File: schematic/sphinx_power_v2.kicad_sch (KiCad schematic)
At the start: 0 parts

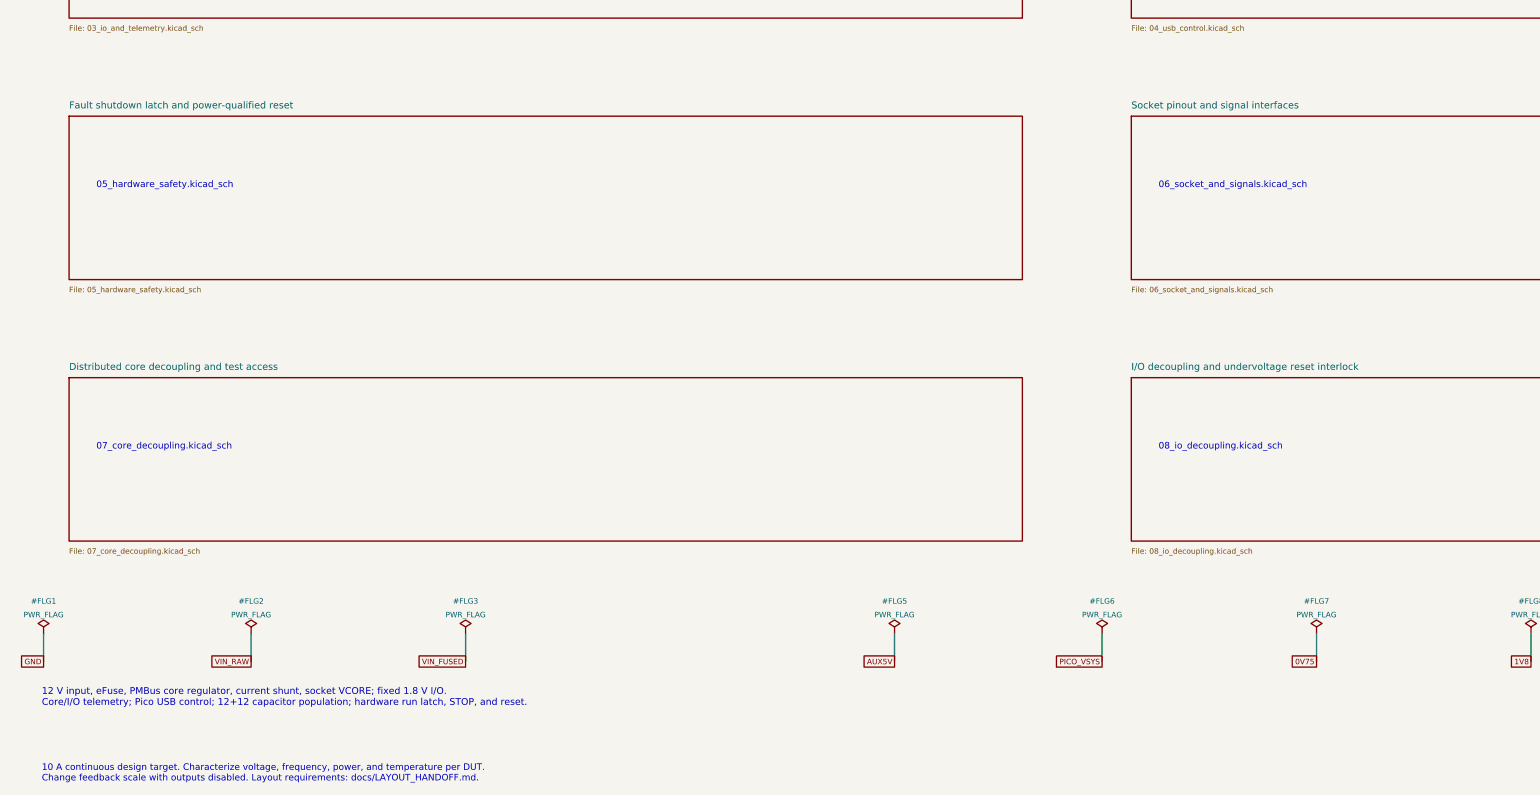
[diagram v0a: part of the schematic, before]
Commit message: Decouple DUT reset and input diagnostics from power interlocks
Use explicit manual, ZedBoard, and Pico reset requests. Route input-voltage validity to telemetry while retaining protective power interlocks. Synchronize requirements, schematic exports, BOM, and verification evidence.
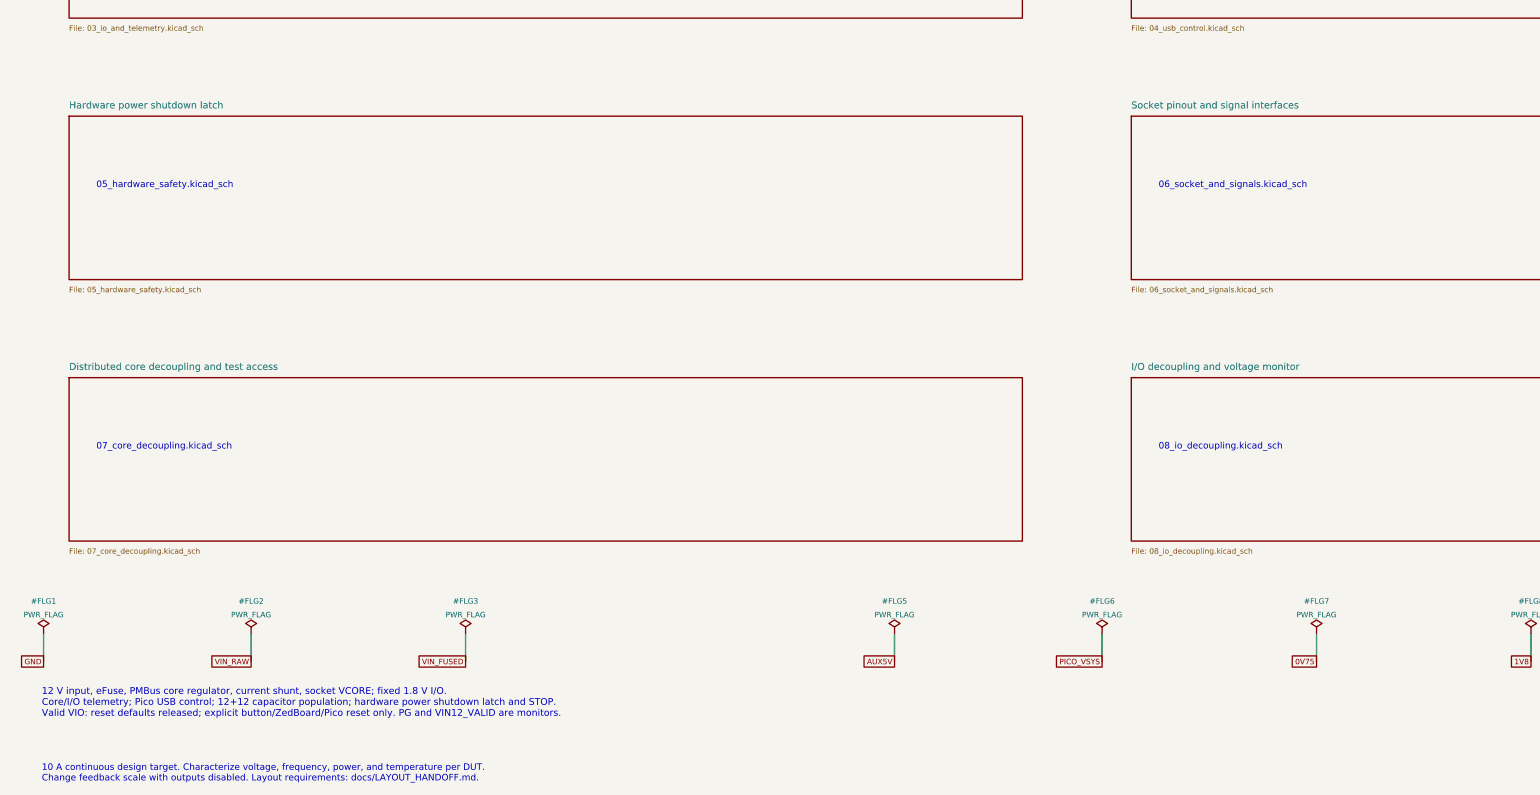
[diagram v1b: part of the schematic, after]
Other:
- sheet Fault shutdown latch and power-qualified reset renamed Hardware power shutdown latch
- sheet I/O decoupling and undervoltage reset interlock renamed I/O decoupling and voltage monitor
- note added: "12 V input, eFuse, PMBus core regulator, current shunt, socket VCORE; fixed 1.8 V I/O. Core/I/O telemetry; Pico USB control; 12+12 capacitor population; hardware power shutdown latch and STOP. Valid VIO: reset defaults released; explicit button/ZedBoard/Pico reset only. PG and VIN12_VALID are monitors."
- note removed: "12 V input, eFuse, PMBus core regulator, current shunt, socket VCORE; fixed 1.8 V I/O. Core/I/O telemetry; Pico USB control; 12+12 capacitor population; hardware run latch, STOP, and reset."
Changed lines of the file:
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@@
 (kicad_sch (version 20250114) (generator "eeschema") (generator_version "10.0")
  (paper "A3")
-        (title_block (title "Sphinx V2 | Programmable power test platform") (date "2026-09-19") (rev "V2")
+        (title_block (title "Sphinx V2 | Programmable power test platform") (date "2026-09-20") (rev "V2")
         (company "Sphinx | Programmable power test board")
         (comment 1 "Review package: PCB, PI, SI, thermal and ASIC limits require qualification")
@@
 (sheet (at 220 97) (size 175 30) (stroke (width 0.254) (type default)) (fill (color 0 0 0 0)) (property "Sheetname" "USB control and remote reset" (at 220 95.73 0) (effects (font (size 1.27 1.27)) (justify left bottom) )) (property "Sheetfile" "04_usb_control.kicad_sch" (at 220 128.27 0) (effects (font (size 1.0 1.0)) (justify left top) )) (instances (project "sphinx_power_v2" (path "/f39c8d6a-e478-5a84-9c95-766dfa82ae02" (page "5")))))
 (text "04_usb_control.kicad_sch" (at 225 109 0) (effects (font (size 1.2 1.2)) (justify left top) ))
-(sheet (at 25 145) (size 175 30) (stroke (width 0.254) (type default)) (fill (color 0 0 0 0)) (property "Sheetname" "Fault shutdown latch and power-qualified reset" (at 25 143.73 0) (effects (font (size 1.27 1.27)) (justify left bottom) )) (property "Sheetfile" "05_hardware_safety.kicad_sch" (at 25 176.27 0) (effects (font (size 1.0 1.0)) (justify left top) )) (instances (project "sphinx_power_v2" (path "/f39c8d6a-e478-5a84-9c95-766dfa82ae02" (page "6")))))
+(sheet (at 25 145) (size 175 30) (stroke (width 0.254) (type default)) (fill (color 0 0 0 0)) (property "Sheetname" "Hardware power shutdown latch" (at 25 143.73 0) (effects (font (size 1.27 1.27)) (justify left bottom) )) (property "Sheetfile" "05_hardware_safety.kicad_sch" (at 25 176.27 0) (effects (font (size 1.0 1.0)) (justify left top) )) (instances (project "sphinx_power_v2" (path "/f39c8d6a-e478-5a84-9c95-766dfa82ae02" (page "6")))))
 (text "05_hardware_safety.kicad_sch" (at 30 157 0) (effects (font (size 1.2 1.2)) (justify left top) ))
 (sheet (at 220 145) (size 175 30) (stroke (width 0.254) (type default)) (fill (color 0 0 0 0)) (property "Sheetname" "Socket pinout and signal interfaces" (at 220 143.73 0) (effects (font (size 1.27 1.27)) (justify left bottom) )) (property "Sheetfile" "06_socket_and_signals.kicad_sch" (at 220 176.27 0) (effects (font (size 1.0 1.0)) (justify left top) )) (instances (project "sphinx_power_v2" (path "/f39c8d6a-e478-5a84-9c95-766dfa82ae02" (page "7")))))
@@
 (sheet (at 25 193) (size 175 30) (stroke (width 0.254) (type default)) (fill (color 0 0 0 0)) (property "Sheetname" "Distributed core decoupling and test access" (at 25 191.73 0) (effects (font (size 1.27 1.27)) (justify left bottom) )) (property "Sheetfile" "07_core_decoupling.kicad_sch" (at 25 224.27 0) (effects (font (size 1.0 1.0)) (justify left top) )) (instances (project "sphinx_power_v2" (path "/f39c8d6a-e478-5a84-9c95-766dfa82ae02" (page "8")))))
 (text "07_core_decoupling.kicad_sch" (at 30 205 0) (effects (font (size 1.2 1.2)) (justify left top) ))
-(sheet (at 220 193) (size 175 30) (stroke (width 0.254) (type default)) (fill (color 0 0 0 0)) (property "Sheetname" "I/O decoupling and undervoltage reset interlock" (at 220 191.73 0) (effects (font (size 1.27 1.27)) (justify left bottom) )) (property "Sheetfile" "08_io_decoupling.kicad_sch" (at 220 224.27 0) (effects (font (size 1.0 1.0)) (justify left top) )) (instances (project "sphinx_power_v2" (path "/f39c8d6a-e478-5a84-9c95-766dfa82ae02" (page "9")))))
+(sheet (at 220 193) (size 175 30) (stroke (width 0.254) (type default)) (fill (color 0 0 0 0)) (property "Sheetname" "I/O decoupling and voltage monitor" (at 220 191.73 0) (effects (font (size 1.27 1.27)) (justify left bottom) )) (property "Sheetfile" "08_io_decoupling.kicad_sch" (at 220 224.27 0) (effects (font (size 1.0 1.0)) (justify left top) )) (instances (project "sphinx_power_v2" (path "/f39c8d6a-e478-5a84-9c95-766dfa82ae02" (page "9")))))
 (text "08_io_decoupling.kicad_sch" (at 225 205 0) (effects (font (size 1.2 1.2)) (justify left top) ))
-(text "12 V input, eFuse, PMBus core regulator, current shunt, socket VCORE; fixed 1.8 V I/O.\nCore/I/O telemetry; Pico USB control; 12+12 capacitor population; hardware run latch, STOP, and reset." (at 20 250 0) (effects (font (size 1.25 1.25)) (justify left top) ))
+(text "12 V input, eFuse, PMBus core regulator, current shunt, socket VCORE; fixed 1.8 V I/O.\nCore/I/O telemetry; Pico USB control; 12+12 capacitor population; hardware power shutdown latch and STOP.\nValid VIO: reset defaults released; explicit button/ZedBoard/Pico reset only. PG and VIN12_VALID are monitors." (at 20 250 0) (effects (font (size 1.25 1.25)) (justify left top) ))
 (text "10 A continuous design target. Characterize voltage, frequency, power, and temperature per DUT.\nChange feedback scale with outputs disabled. Layout requirements: docs/LAYOUT_HANDOFF.md." (at 20 264 0) (effects (font (size 1.2 1.2)) (justify left top) ))
 (symbol (lib_id "Sphinx_V2:power__PWR_FLAG") (at 20.32 240.03 0) (unit 1) (exclude_from_sim no) (in_bom yes) (on_board yes) (dnp no)

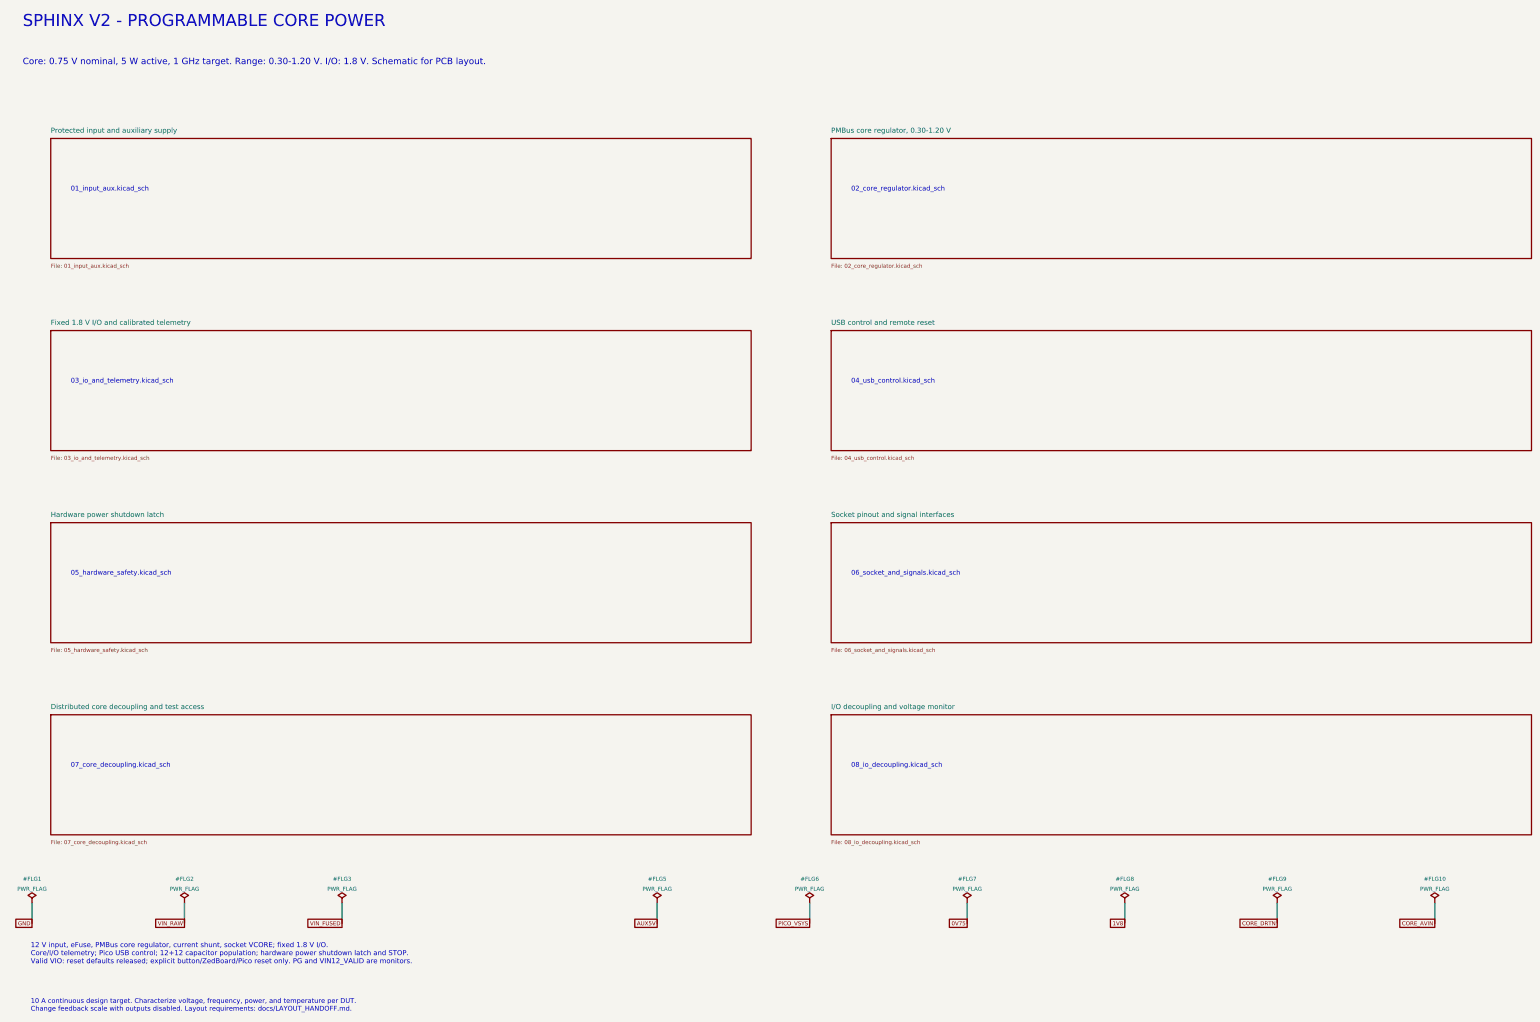
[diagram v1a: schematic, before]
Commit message: Make V2 power state independent of Pico
Add an independently powered retained control domain, isolated I2C, hardware temperature and I/O overvoltage protection, and correct the socket keepout. Align operating requirements, BOM, schematic exports, and validation evidence.

Complete the final source review: zero ERC violations, 247 footprint/BOM matches, 80 ASIC pin checks, and 51 companion host tests including 122 interrupted-write cases. Record physical qualification limits and external companion firmware hashes.
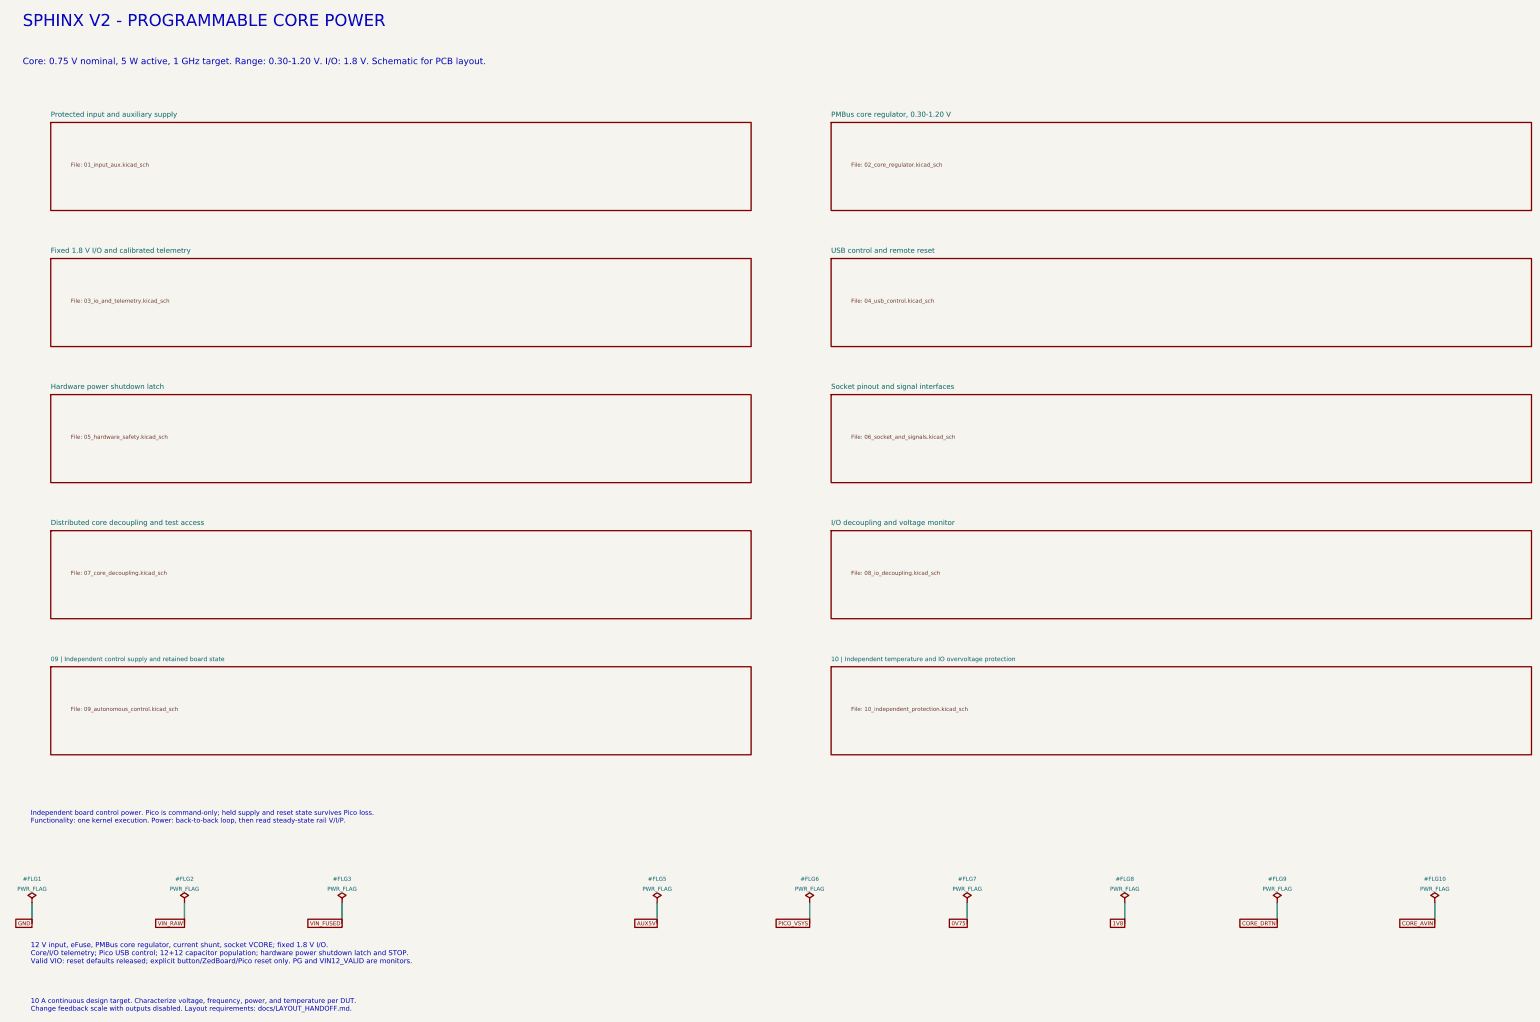
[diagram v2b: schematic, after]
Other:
- added sheet 09 | Independent control supply and retained board state (09_autonomous_control.kicad_sch)
- added sheet 10 | Independent temperature and IO overvoltage protection (10_independent_protection.kicad_sch)
- note added: "Independent board control power. Pico is command-only; held supply and reset state survives Pico loss. Functionality: one kernel execution. Power: back-to-back loop, then read steady-state rail V/I/P."
- note removed: "01_input_aux.kicad_sch"
- note removed: "02_core_regulator.kicad_sch"
- note removed: "03_io_and_telemetry.kicad_sch"
- note removed: "04_usb_control.kicad_sch"
- note removed: "05_hardware_safety.kicad_sch"
- note removed: "06_socket_and_signals.kicad_sch"
- note removed: "07_core_decoupling.kicad_sch"
- note removed: "08_io_decoupling.kicad_sch"
